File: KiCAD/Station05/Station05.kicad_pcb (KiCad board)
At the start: 4 copper layers, 98 x 49 mm, 11 parts, among them U1 CON-SMA-EDGE, U10 CON-SMA-EDGE, U11 LSHM-110-02.5-L-DV-A-S-TR, U2 CON-SMA-EDGE, U3 CON-SMA-EDGE, U4 CON-SMA-EDGE, U5 CON-SMA-EDGE, U6 CON-SMA-EDGE, U7 CON-SMA-EDGE, U8 CON-SMA-EDGE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

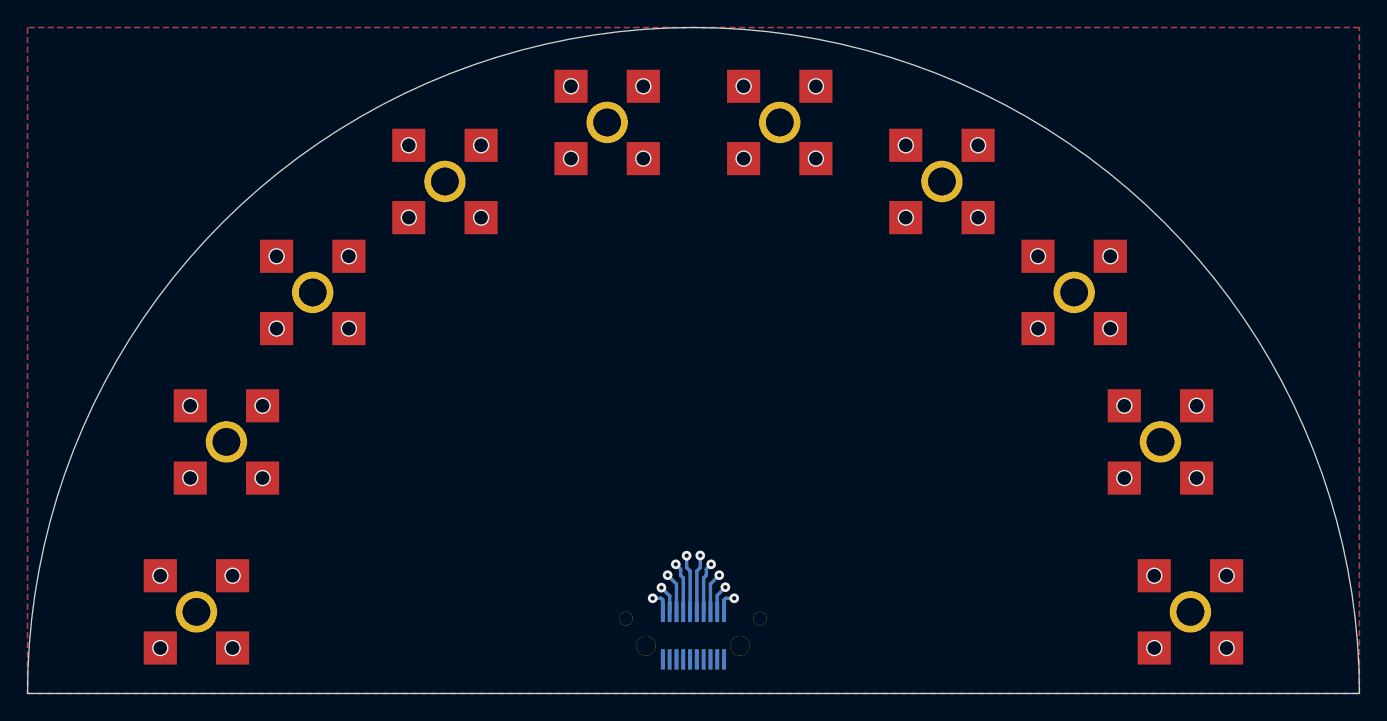
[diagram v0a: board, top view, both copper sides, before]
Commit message: finished station04 and station05
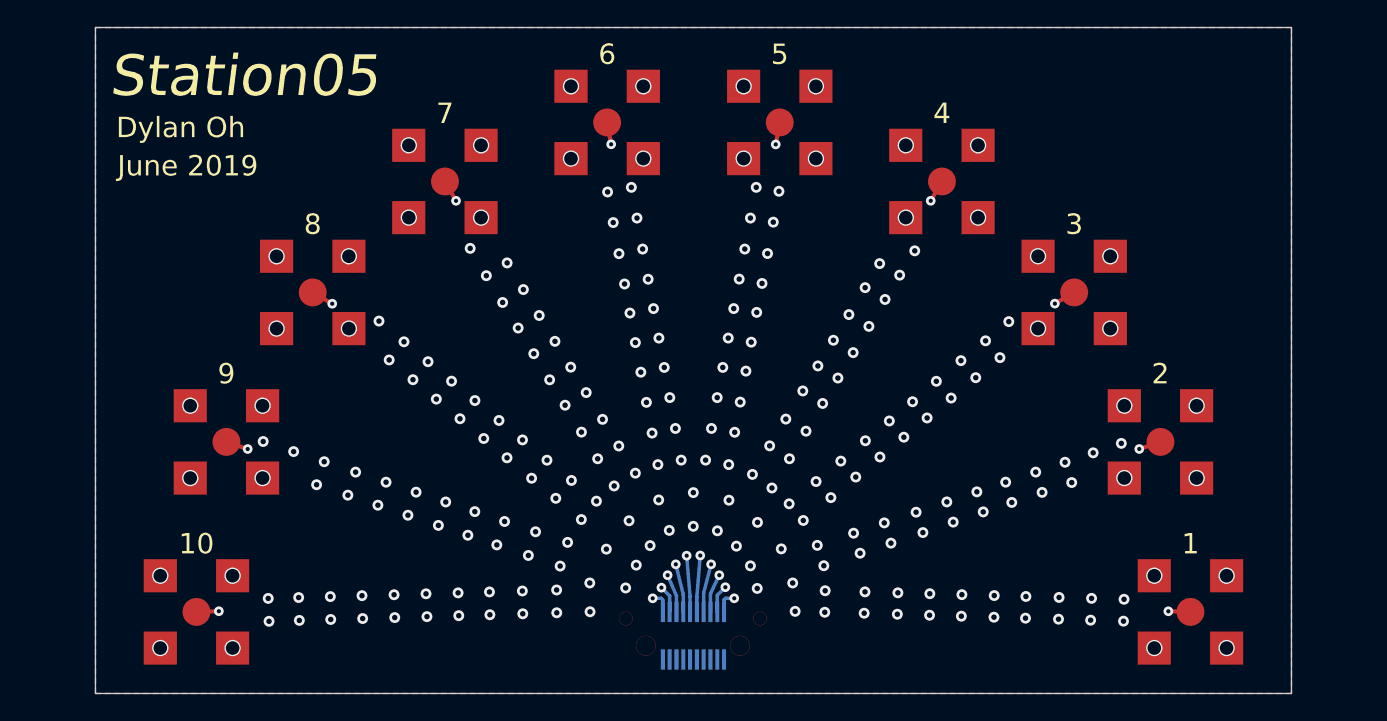
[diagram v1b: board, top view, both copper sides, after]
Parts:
- U1, U10, U2, U3, U4, U5, U6, U7, U8, U9: value CON-SMA-EDGE -> CONSMA001-SMD-G; footprint StationXX:CONSMA001-SMD-G -> Station05:CONSMA001-SMD-G
- U11: footprint StationXX:LSHM-110-02.5-L-DV-A-S-TR -> Station05:LSHM-110-02.5-L-DV-A-S-TR
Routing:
- net Net-(U11-Pad4): track 2.03 -> 35.8 mm, vias 1 -> 2
- net Net-(U11-Pad18): track 2.06 -> 35.8 mm, vias 1 -> 2
- net Net-(U10-Pad1): track 1.68 -> 35.3 mm, vias 1 -> 2
- net Net-(U1-Pad1): track 1.67 -> 35.3 mm, vias 1 -> 2
- net Net-(U11-Pad16): track 2.97 -> 36.3 mm, vias 1 -> 2
- net Net-(U11-Pad6): track 2.97 -> 36.3 mm, vias 1 -> 2
- net Net-(U11-Pad14): track 3.73 -> 36.5 mm, vias 1 -> 2
- net Net-(U11-Pad8): track 3.73 -> 36.5 mm, vias 1 -> 2
- net Net-(U11-Pad10): track 4.24 -> 36.6 mm, vias 1 -> 2
- net Net-(U11-Pad12): track 4.25 -> 36.6 mm, vias 1 -> 2
- net GND: track 0.00 -> 0.04 mm, vias 40 -> 256
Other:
- board size 98 x 49 mm -> 88 x 49 mm
- board text added: "1"
- board text added: "10"
- board text added: "2"
- board text added: "3"
- board text added: "4"
- board text added: "5"
- board text added: "6"
- board text added: "7"
- board text added: "8"
- board text added: "9"
- board text added: "Dylan Oh"
- board text added: "June 2019"
- board text added: "Station05"
